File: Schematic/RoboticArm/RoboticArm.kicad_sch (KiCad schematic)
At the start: 46 parts, among them M1 Motor_Servo, M2 Motor_Servo, M3 Motor_Servo, M4 Motor_Servo, U1 Pico, U2 LM358, U3 LM358, U4 LM358, U5 LM358, U6 LM358

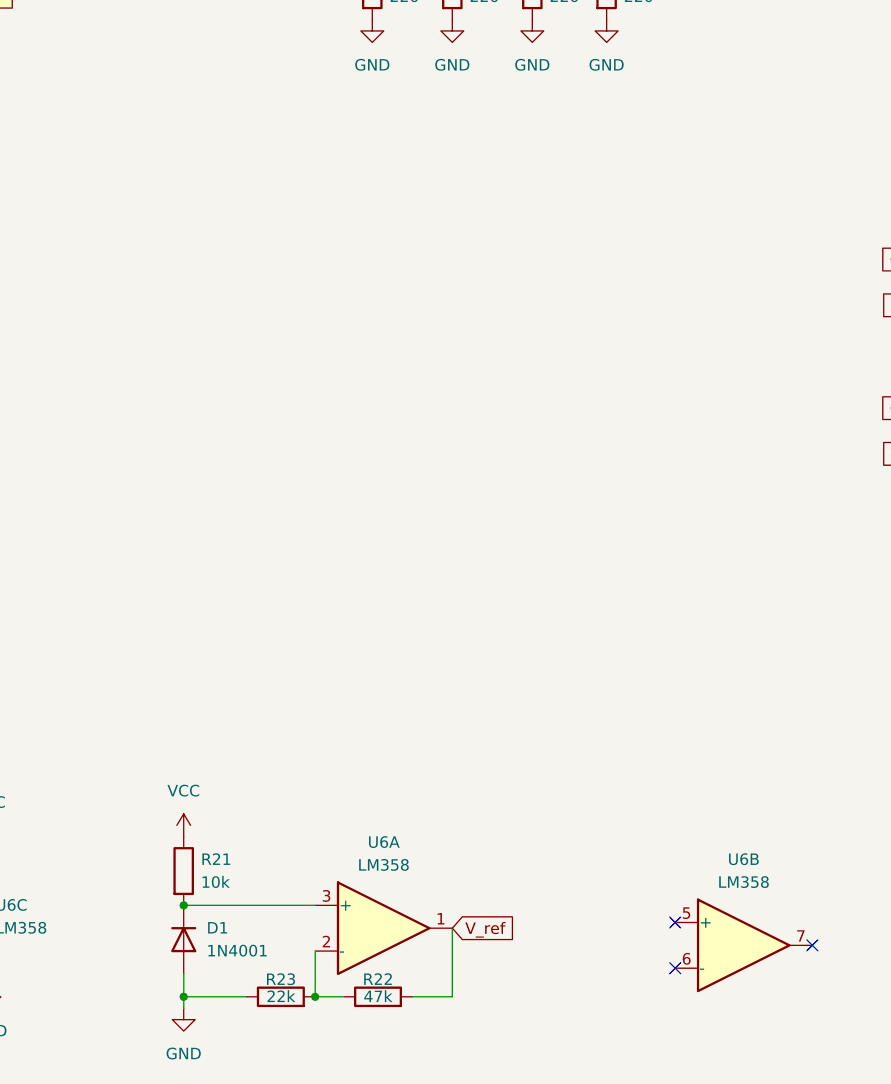
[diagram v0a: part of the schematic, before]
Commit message: Correcting typos
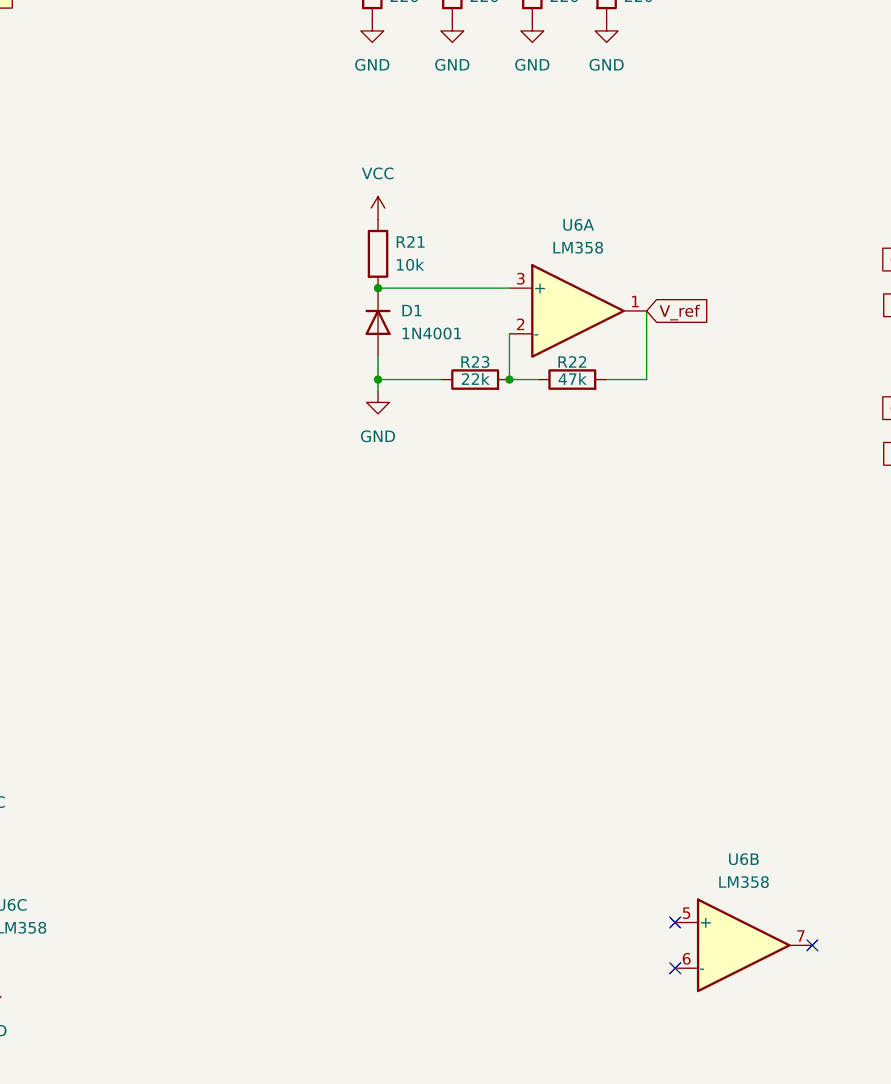
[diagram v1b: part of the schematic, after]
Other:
- company: (none) -> Łukasz Przystupa
- title: (none) -> Robotic Arm
- moved on the sheet: D1, R21, R22, R23, U6A
